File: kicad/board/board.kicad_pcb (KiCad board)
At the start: 2 copper layers, 126.9 x 103.7 mm, 39 parts

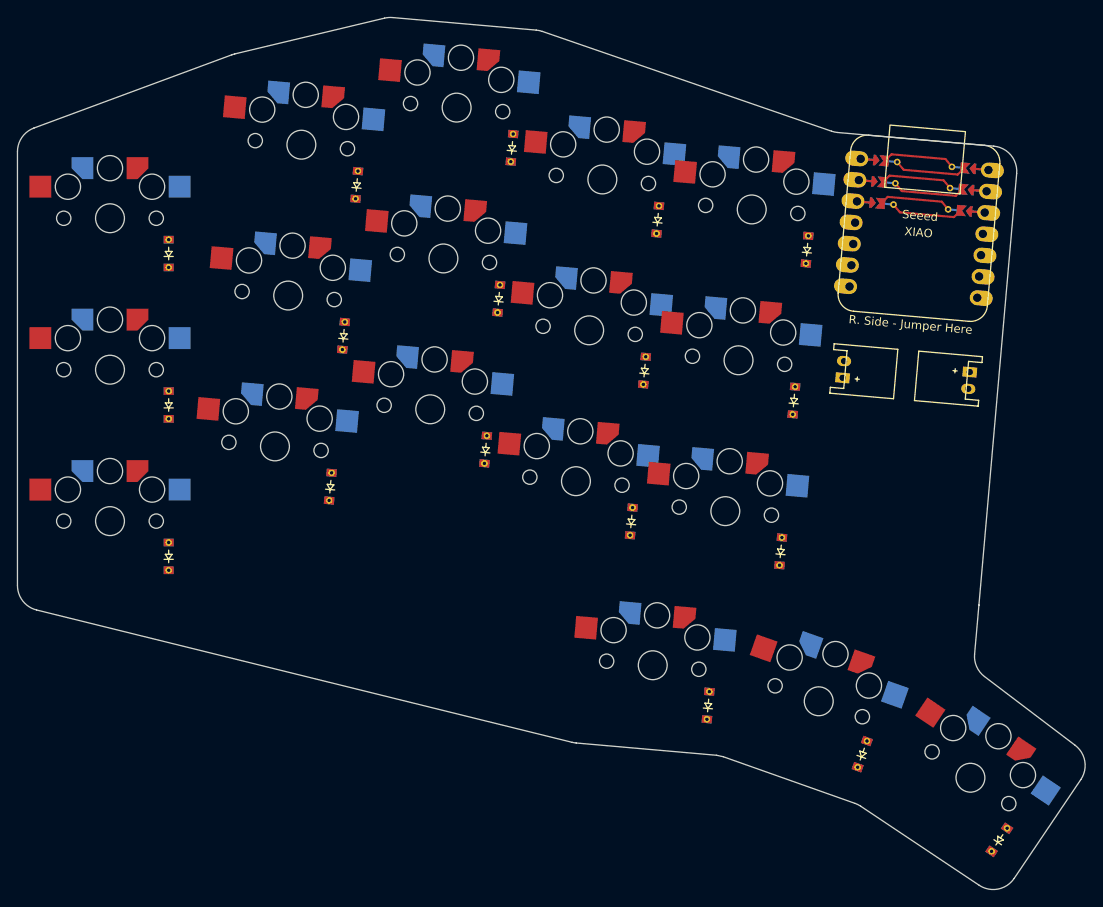
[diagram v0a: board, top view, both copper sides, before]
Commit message: added mounting holes
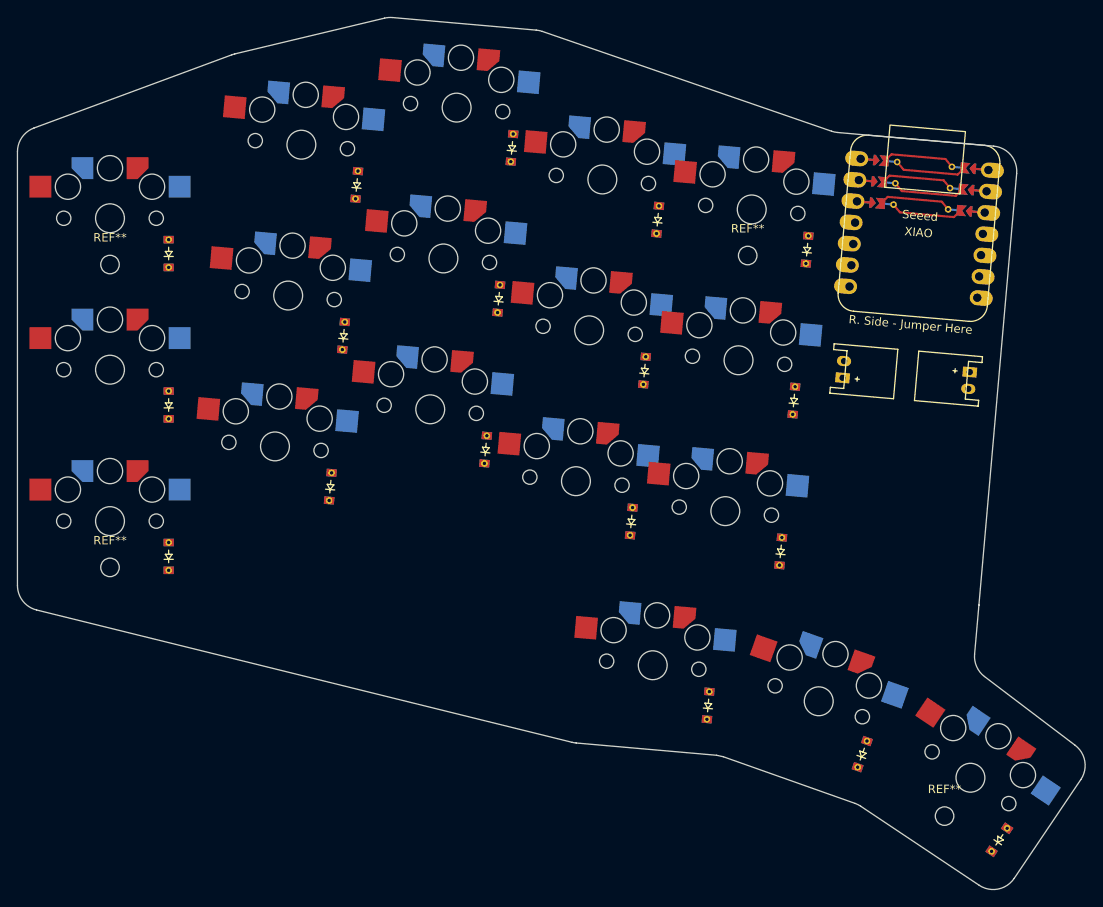
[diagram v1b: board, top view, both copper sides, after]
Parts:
- added REF**: MountingHole_2.2mm_M2, MountingHole:MountingHole_2.2mm_M2, F.Cu at (0.00, -30.5)
- added REF**: MountingHole_2.2mm_M2, MountingHole:MountingHole_2.2mm_M2, F.Cu at (99.2, 35.1)
- added REF**: MountingHole_2.2mm_M2, MountingHole:MountingHole_2.2mm_M2, F.Cu at (75.8, -31.6)
- added REF**: MountingHole_2.2mm_M2, MountingHole:MountingHole_2.2mm_M2, F.Cu at (0.00, 5.50)
